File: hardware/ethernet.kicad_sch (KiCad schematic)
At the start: 2 parts, among them U3 RTL8211F-CG

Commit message: stuff
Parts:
- removed RJ1: HR911130A, easyeda2kicad:RJ45-TH_HR911130A, symbol easyeda2kicad:HR911130A
- removed U3: RTL8211F-CG, Package_DFN_QFN:VQFN-40-1EP_5x5mm_P0.4mm_EP3.7x3.7mm, symbol easyeda2kicad:RTL8211F-CG
- added C53, C54: 100n, Capacitor_SMD:C_0201_0603Metric, symbol Device:C_Small
- added J1: RJ45_Hanrun_HR911105A_Horizontal, Connector_RJ:RJ45_Hanrun_HR911105A_Horizontal, symbol Connector:RJ45_Hanrun_HR911105A_Horizontal
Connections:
- new net: C54.2, J1.5 (RCT)
- new net: C53.2, J1.4 (TCT)
- new net +3V3: J1.12, J1.9
- new net GND: C53.1, C54.1, J1.8, J1.SH
- new net PHY_DATA_LED: J1.11
- new net PHY_LINK_LED: J1.10
- new net PHY_RXN: J1.6 (RD-)
- new net PHY_RXP: J1.3 (RD+)
- new net PHY_TXN: J1.2 (TD-)
- new net PHY_TXP: J1.1 (TD+)

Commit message: Routing and PCB
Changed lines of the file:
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@@
-		)
-	)
-	(label "{PHY_RXN PHY_RXP PHY_TXP PHY_TXN PHY_LINK_LED PHY_DATA_LED}"
-		(at 133.35 95.25 270)
-		(effects
-			(font
-				(size 1.27 1.27)
-			)
-			(justify right bottom)
 		)
 	)
@@
 		)
 	)
+	(label "{FEPHY}"
+		(at 133.35 107.95 270)
+		(effects
+			(font
+				(size 1.27 1.27)
+			)
+			(justify right bottom)
+		)
+	)

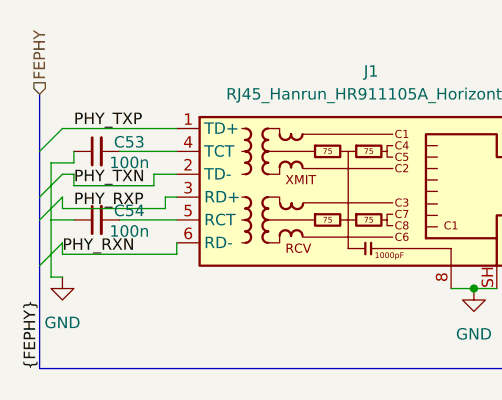
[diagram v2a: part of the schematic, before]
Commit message: component Placement
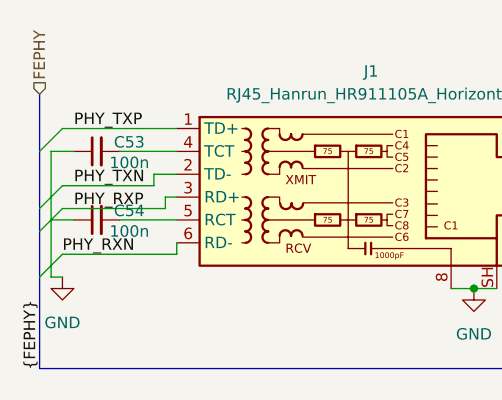
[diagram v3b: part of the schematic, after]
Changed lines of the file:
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@@
 	)
 	(bus_entry
-		(at 133.35 104.14)
+		(at 133.35 105.41)
 		(size 2.54 -2.54)
 		(stroke
@@
 	)
 	(bus_entry
-		(at 133.35 99.06)
-		(size 2.54 -2.54)
-		(stroke
-			(width 0)
-			(type default)
-		)
-	)
-	(bus_entry
-		(at 133.35 96.52)
+		(at 133.35 100.33)
+		(size 2.54 -2.54)
+		(stroke
+			(width 0)
+			(type default)
+		)
+	)
+	(bus_entry
+		(at 133.35 97.79)
 		(size 2.54 -2.54)
 		(stroke
@@
 	(wire
 		(pts
-			(xy 135.89 96.52) (xy 135.89 97.79)
-		)
-		(stroke
-			(width 0)
-			(type default)
-		)
-	)
-	(wire
-		(pts
 			(xy 181.61 106.68) (xy 184.15 106.68)
 		)
@@
 	(wire
 		(pts
-			(xy 135.89 101.6) (xy 135.89 102.87)
-		)
-		(stroke
-			(width 0)
-			(type default)
-		)
-	)
-	(wire
-		(pts
 			(xy 191.77 101.6) (xy 199.39 101.6)
 		)
@@
 	(wire
 		(pts
-			(xy 134.62 92.71) (xy 134.62 99.06)
+			(xy 134.62 91.44) (xy 134.62 99.06)
 		)
 		(stroke
@@
 		)
 	)
+	(bus
+		(pts
+			(xy 133.35 85.09) (xy 133.35 115.57)
+		)
+		(stroke
+			(width 0)
+			(type default)
+		)
+	)
 	(wire
 		(pts
@@
 	(wire
 		(pts
-			(xy 137.16 92.71) (xy 134.62 92.71)
+			(xy 137.16 91.44) (xy 134.62 91.44)
 		)
 		(stroke
@@
 	(wire
 		(pts
-			(xy 137.16 95.25) (xy 146.05 95.25)
-		)
-		(stroke
-			(width 0)
-			(type default)
-		)
-	)
-	(wire
-		(pts
 			(xy 135.89 102.87) (xy 148.59 102.87)
 		)
@@
 	(wire
 		(pts
-			(xy 137.16 91.44) (xy 137.16 92.71)
-		)
-		(stroke
-			(width 0)
-			(type default)
-		)
-	)
-	(wire
-		(pts
 			(xy 146.05 93.98) (xy 148.59 93.98)
 		)
@@
 	(wire
 		(pts
-			(xy 137.16 93.98) (xy 137.16 95.25)
-		)
-		(stroke
-			(width 0)
-			(type default)
-		)
-	)
-	(bus
-		(pts
-			(xy 133.35 85.09) (xy 133.35 115.57)
-		)
-		(stroke
-			(width 0)
-			(type default)
-		)
-	)
-	(wire
-		(pts
-			(xy 135.89 93.98) (xy 137.16 93.98)
-		)
-		(stroke
+			(xy 135.89 95.25) (xy 146.05 95.25)
+		)
+		(stroke

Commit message: final touches
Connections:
- net RCT: now reaches C54.2, J1.5 (RCT)
- net TCT: now reaches C53.2, J1.4 (TCT)
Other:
- moved on the sheet: J1
